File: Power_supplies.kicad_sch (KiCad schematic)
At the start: 54 parts, among them J2 DG35C-B-02P, T1 AOSP21357, T2 MJD32C, U3 MC34063, U31 EL817, U4 MC34063, U5 TLV70233_SOT23-5

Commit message: v2.1 finished
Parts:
- added D101: AOZ8211, _Diodes:AOZ8211, symbol _Diodes:AOZ8211
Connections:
- net 3V3: now also D101.2
- net GND: now also D101.1
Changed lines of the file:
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@@
   (junction (at 182.88 104.14) (diameter 0) (color 0 0 0 0)
   )
+  (junction (at 271.78 62.23) (diameter 0) (color 0 0 0 0)
+  )
   (junction (at 113.03 45.72) (diameter 0) (color 0 0 0 0)
   )
@@
     (stroke (width 0) (type default) (color 0 0 0 0))
   )
+  (wire (pts (xy 271.78 62.23) (xy 276.86 62.23))
+    (stroke (width 0) (type default) (color 0 0 0 0))
+  )
   (wire (pts (xy 138.43 113.03) (xy 135.89 113.03))
     (stroke (width 0) (type default) (color 0 0 0 0))
@@
     (stroke (width 0) (type default) (color 0 0 0 0))
   )
+  (wire (pts (xy 271.78 76.2) (xy 271.78 81.28))
+    (stroke (width 0) (type default) (color 0 0 0 0))
+  )
   (wire (pts (xy 36.83 34.29) (xy 36.83 36.83))
     (stroke (width 0) (type default) (color 0 0 0 0))
@@
     (stroke (width 0) (type default) (color 0 0 0 0))
   )
+  (wire (pts (xy 271.78 62.23) (xy 271.78 68.58))
+    (stroke (width 0) (type default) (color 0 0 0 0))
+  )
   (wire (pts (xy 194.31 62.23) (xy 200.66 62.23))
     (stroke (width 0) (type default) (color 0 0 0 0))
@@
     (stroke (width 0) (type default) (color 0 0 0 0))
   )
-  (wire (pts (xy 256.54 62.23) (xy 266.7 62.23))
+  (wire (pts (xy 256.54 62.23) (xy 271.78 62.23))
     (stroke (width 0) (type default) (color 0 0 0 0))
   )
@@
     (effects (font (size 1.27 1.27)) (justify left))
   )
-  (hierarchical_label "3V3" (shape output) (at 266.7 62.23 0)
+  (hierarchical_label "3V3" (shape output) (at 276.86 62.23 0)
     (effects (font (size 1.27 1.27)) (justify left))
   )
@@
   (symbol (lib_id "Connector:TestPoint") (at 267.97 22.86 0) (unit 1)
     (in_bom yes) (on_board yes)
-    (property "Reference" "TP33" (id 0) (at 269.24 17.78 0)
+    (property "Reference" "TP33" (id 0) (at 267.97 13.97 90)
       (effects (font (size 1.27 1.27)) (justify right))
     )
@@
   (symbol (lib_id "Connector:TestPoint") (at 275.59 22.86 0) (unit 1)
     (in_bom yes) (on_board yes)
-    (property "Reference" "TP41" (id 0) (at 276.86 17.78 0)
+    (property "Reference" "TP41" (id 0) (at 275.59 13.97 90)
       (effects (font (size 1.27 1.27)) (justify right))
     )
@@
   (symbol (lib_id "Connector:TestPoint") (at 264.16 22.86 0) (unit 1)
     (in_bom yes) (on_board yes)
-    (property "Reference" "TP32" (id 0) (at 265.43 17.78 0)
+    (property "Reference" "TP32" (id 0) (at 264.16 13.97 90)
       (effects (font (size 1.27 1.27)) (justify right))
     )
@@
   (symbol (lib_id "Connector:TestPoint") (at 279.4 22.86 0) (unit 1)
     (in_bom yes) (on_board yes)
-    (property "Reference" "TP48" (id 0) (at 280.67 17.78 0)
+    (property "Reference" "TP48" (id 0) (at 279.4 13.97 90)
       (effects (font (size 1.27 1.27)) (justify right))
     )
@@
     )
     (property "Datasheet" "~" (id 3) (at 284.48 22.86 0)
+      (effects (font (size 1.27 1.27)) hide)
+    )
+    (pin "1")
+  )
+  (symbol (lib_id "power:GND") (at 271.78 81.28 0) (unit 1)
+    (in_bom yes) (on_board yes) (fields_autoplaced)
+    (property "Reference" "#PWR0210" (id 0) (at 271.78 87.63 0)
+      (effects (font (size 1.27 1.27)) hide)
+    )
+    (property "Value" "GND" (id 1) (at 271.78 86.36 0))
+    (property "Footprint" "" (id 2) (at 271.78 81.28 0)
+      (effects (font (size 1.27 1.27)) hide)
+    )
+    (property "Datasheet" "" (id 3) (at 271.78 81.28 0)
       (effects (font (size 1.27 1.27)) hide)
     )
@@
   (symbol (lib_id "Connector:TestPoint") (at 271.78 22.86 0) (unit 1)
     (in_bom yes) (on_board yes)
-    (property "Reference" "TP40" (id 0) (at 273.05 17.78 0)
+    (property "Reference" "TP40" (id 0) (at 271.78 13.97 90)
       (effects (font (size 1.27 1.27)) (justify right))
     )
@@
       (effects (font (size 1.27 1.27)) hide)
     )
+    (pin "1")
+    (pin "2")
+  )
+  (symbol (lib_id "_Diodes:AOZ8211") (at 269.24 72.39 90) (unit 1)
+    (in_bom yes) (on_board yes) (fields_autoplaced)
+    (property "Reference" "D101" (id 0) (at 274.32 71.1199 90)
+      (effects (font (size 1.27 1.27)) (justify right))
+    )
+    (property "Value" "AOZ8211" (id 1) (at 274.32 73.6599 90)
+      (effects (font (size 1.27 1.27)) (justify right))
+    )
+    (property "Footprint" "_Diodes:AOZ8211" (id 2) (at 269.24 72.39 0)
+      (effects (font (size 1.27 1.27)) hide)
+    )
+    (property "Datasheet" "" (id 3) (at 269.24 72.39 0)
+      (effects (font (size 1.27 1.27)) hide)
+    )

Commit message: changed power loss detection schematic, changed tvs diodes on other type, added two more caps on 3v3 line, change indicator leds resistors
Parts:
- removed D101: AOZ8211, _Diodes:AOZ8211, symbol _Diodes:AOZ8211
- removed R108, R109: 1k, Resistor_SMD:R_0603_1608Metric_Pad0.98x0.95mm_HandSolder, symbol Device:R
- removed TP9, TP93: TestPoint, TestPoint:TestPoint_THTPad_1.0x1.0mm_Drill0.5mm, symbol Connector:TestPoint
- removed U31: EL817, Package_DIP:DIP-4_W8.89mm_SMDSocket_LongPads, symbol Isolator:EL817
- added C?: 220u, Capacitor_SMD:CP_Elec_6.3x5.4, symbol Device:C_Polarized
- added C? (x2): 330u 6.3V, Capacitor_SMD:CP_Elec_8x6.2, symbol Device:C_Polarized
- added D?: UCLAMP3301D.TCT, _Diodes:UCLAMP3301D.TCT, symbol _Diodes:UCLAMP3301D.TCT
- added D?: B330, Diode_SMD:D_SMA_Handsoldering, symbol Diode:B330
- added R: 100k, Resistor_SMD:R_0603_1608Metric_Pad0.98x0.95mm_HandSolder, symbol Device:R
- added R?: 47k, Resistor_SMD:R_0603_1608Metric_Pad0.98x0.95mm_HandSolder, symbol Device:R
- added R?: 10k, Resistor_SMD:R_0603_1608Metric_Pad0.98x0.95mm_HandSolder, symbol Device:R
- added TP?: TestPoint, TestPoint:TestPoint_THTPad_1.0x1.0mm_Drill0.5mm, symbol Connector:TestPoint
- added U? (x2): AP331A, symbol _IntegratedCircuits:AP331A
- C14: value 100u -> 330u 6.3V
- R12: value 10k -> 36k
- R15: value 3k -> 12k
- R16, R2: value 15k -> 36k
- R6: value 240 -> 240R
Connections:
- net +3V3: now also D?.2 (A), R?.1, U?.5 (V+)
- net 3V3: now also C?.1, C?.1, D?.1
- net GND: now also C?.2, C?.2, C?.2, D?.2, R?.2, U?.2 (V-)
- net POWER_ERROR: now also R?.2, TP?.1, U?.4
- net VDD: now also R.1
- new net 3V_inverting_in: C?.1, D?.1 (K), U?.1 (-)
- new net divider_non_inverting_in: R.2, R?.1, U?.3 (+)
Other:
- note added: "3,3V 300mA"
- note added: "3V"
- note added: "HI - POWER LOSS NOT DETECTED LO - POWER LOSS DETECTED"
- note added: "Open colllector output"
- note added: "~9.5V on power line = power loss detected"
- note removed: "3,3V 200mA"
- note removed: "HI - POWER OFF LO - POWER ON"
- moved on the sheet: C14

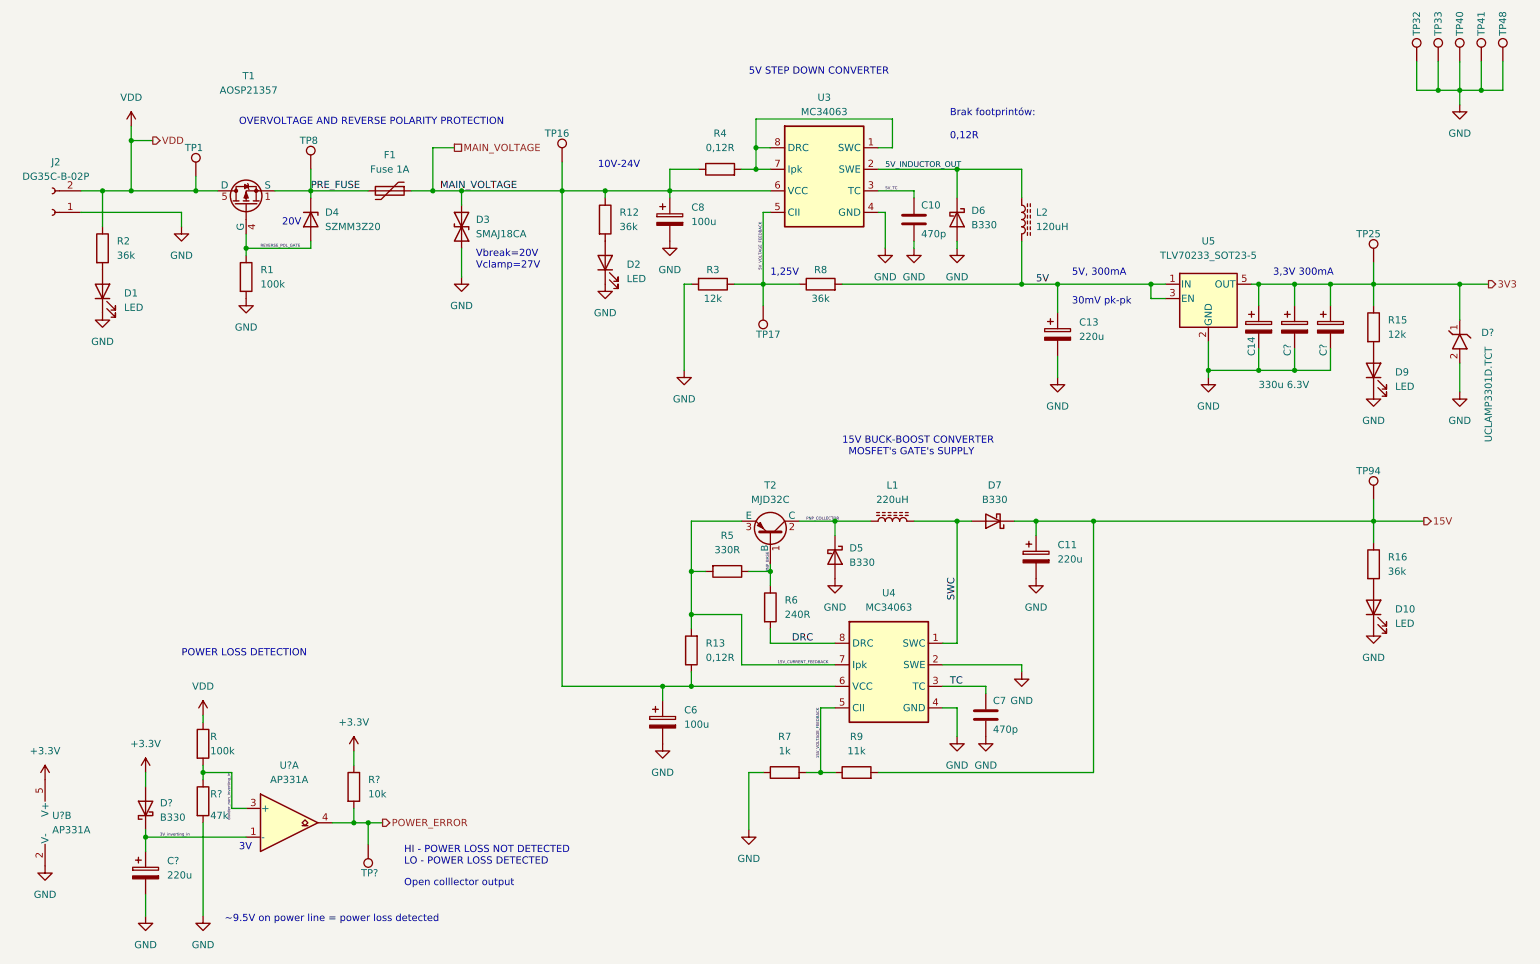
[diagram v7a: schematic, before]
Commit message: updated footprints on board and sgematics
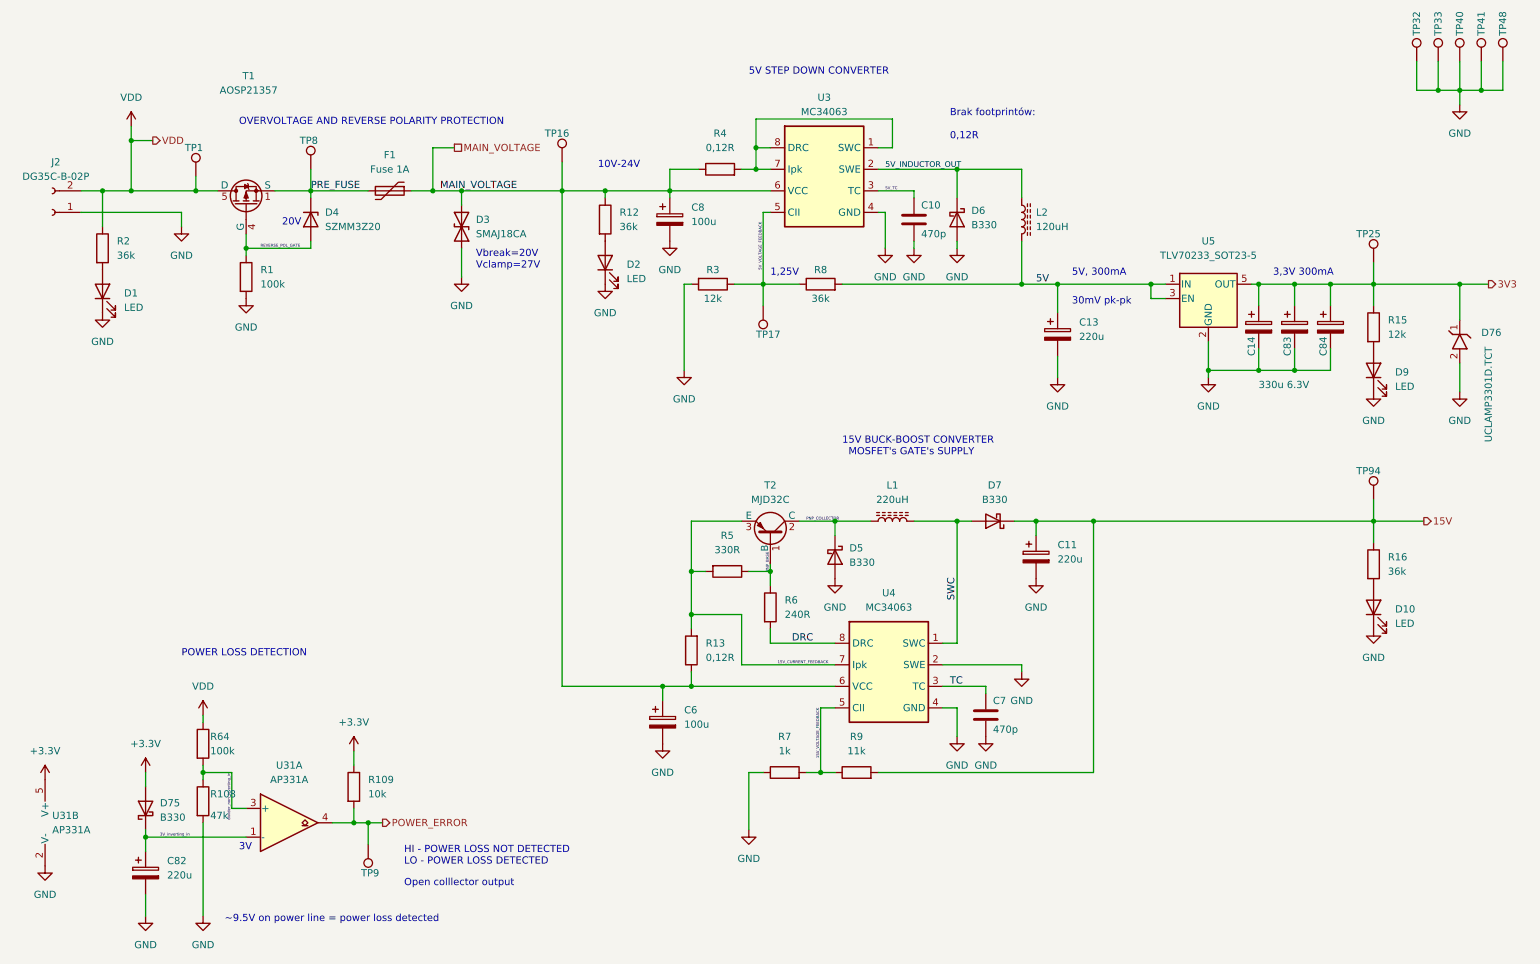
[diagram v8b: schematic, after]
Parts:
- D3: footprint Diode_SMD:D_SMA_Handsoldering -> Diode_THT:D_DO-201AE_P15.24mm_Horizontal
- D5, D6, D7: footprint Diode_SMD:D_SMA_Handsoldering -> Diode_SMD:D_SMC
- D75: renamed from D?; footprint Diode_SMD:D_SMA_Handsoldering -> Diode_SMD:D_SMC
- gave numbers to parts that had none: 8
- renumbered R to R64
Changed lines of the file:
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@@
       (effects (font (size 1.27 1.27)) (justify right))
     )
-    (property "Footprint" "Diode_SMD:D_SMA_Handsoldering" (id 2) (at 100.33 52.07 0)
+    (property "Footprint" "Diode_THT:D_DO-201AE_P15.24mm_Horizontal" (id 2) (at 100.33 52.07 0)
       (effects (font (size 1.27 1.27)) hide)
     )
@@
       (effects (font (size 1.27 1.27)) (justify left))
     )
-    (property "Footprint" "Diode_SMD:D_SMA_Handsoldering" (id 2) (at 156.845 110.49 0)
+    (property "Footprint" "Diode_SMD:D_SMC" (id 2) (at 156.845 110.49 0)
       (effects (font (size 1.27 1.27)) hide)
     )
@@
   (symbol (lib_id "power:VDD") (at 49.53 138.43 0) (unit 1)
     (in_bom yes) (on_board yes) (fields_autoplaced)
-    (property "Reference" "#PWR?" (id 0) (at 49.53 142.24 0)
+    (property "Reference" "#PWR0188" (id 0) (at 49.53 142.24 0)
       (effects (font (size 1.27 1.27)) hide)
     )
@@
   (symbol (lib_id "power:+3.3V") (at 39.37 148.59 0) (unit 1)
     (in_bom yes) (on_board yes) (fields_autoplaced)
-    (property "Reference" "#PWR?" (id 0) (at 39.37 152.4 0)
+    (property "Reference" "#PWR0215" (id 0) (at 39.37 152.4 0)
       (effects (font (size 1.27 1.27)) hide)
     )
@@
   (symbol (lib_id "_IntegratedCircuits:AP331A") (at 21.59 157.48 0) (unit 2)
     (in_bom yes) (on_board yes) (fields_autoplaced)
-    (property "Reference" "U?" (id 0) (at 22.86 156.2099 0)
+    (property "Reference" "U31" (id 0) (at 22.86 156.2099 0)
       (effects (font (size 1.27 1.27)) (justify left))
     )
@@
   (symbol (lib_id "Device:C_Polarized") (at 39.37 166.37 0) (unit 1)
     (in_bom yes) (on_board yes) (fields_autoplaced)
-    (property "Reference" "C?" (id 0) (at 43.18 164.2109 0)
+    (property "Reference" "C82" (id 0) (at 43.18 164.2109 0)
       (effects (font (size 1.27 1.27)) (justify left))
     )
@@
   (symbol (lib_id "power:GND") (at 49.53 173.99 0) (unit 1)
     (in_bom yes) (on_board yes) (fields_autoplaced)
-    (property "Reference" "#PWR?" (id 0) (at 49.53 180.34 0)
+    (property "Reference" "#PWR0191" (id 0) (at 49.53 180.34 0)
       (effects (font (size 1.27 1.27)) hide)
     )
@@
   (symbol (lib_id "power:GND") (at 21.59 165.1 0) (unit 1)
     (in_bom yes) (on_board yes) (fields_autoplaced)
-    (property "Reference" "#PWR?" (id 0) (at 21.59 171.45 0)
+    (property "Reference" "#PWR0217" (id 0) (at 21.59 171.45 0)
       (effects (font (size 1.27 1.27)) hide)
     )
@@
   (symbol (lib_id "power:+3.3V") (at 21.59 149.86 0) (unit 1)
     (in_bom yes) (on_board yes) (fields_autoplaced)
-    (property "Reference" "#PWR?" (id 0) (at 21.59 153.67 0)
+    (property "Reference" "#PWR0216" (id 0) (at 21.59 153.67 0)
       (effects (font (size 1.27 1.27)) hide)
     )
@@
   (symbol (lib_id "Device:C_Polarized") (at 248.92 69.85 0) (unit 1)
     (in_bom yes) (on_board yes)
-    (property "Reference" "C?" (id 0) (at 247.65 74.93 90)
+    (property "Reference" "C84" (id 0) (at 247.65 74.93 90)
       (effects (font (size 1.27 1.27)) (justify left))
     )
@@
   (symbol (lib_id "power:GND") (at 39.37 173.99 0) (unit 1)
     (in_bom yes) (on_board yes) (fields_autoplaced)
-    (property "Reference" "#PWR?" (id 0) (at 39.37 180.34 0)
+    (property "Reference" "#PWR0190" (id 0) (at 39.37 180.34 0)
       (effects (font (size 1.27 1.27)) hide)
     )
@@
   (symbol (lib_id "Device:R") (at 49.53 153.67 0) (unit 1)
     (in_bom yes) (on_board yes)
-    (property "Reference" "R?" (id 0) (at 50.8 152.4 0)
+    (property "Reference" "R108" (id 0) (at 50.8 152.4 0)
       (effects (font (size 1.27 1.27)) (justify left))
     )
@@
   (symbol (lib_id "Device:R") (at 49.53 143.51 0) (unit 1)
     (in_bom yes) (on_board yes)
-    (property "Reference" "R" (id 0) (at 50.8 142.24 0)
+    (property "Reference" "R64" (id 0) (at 50.8 142.24 0)
       (effects (font (size 1.27 1.27)) (justify left))
     )
@@
   (symbol (lib_id "power:+3.3V") (at 76.2 144.78 0) (unit 1)
     (in_bom yes) (on_board yes) (fields_autoplaced)
-    (property "Reference" "#PWR?" (id 0) (at 76.2 148.59 0)
+    (property "Reference" "#PWR0189" (id 0) (at 76.2 148.59 0)
       (effects (font (size 1.27 1.27)) hide)
     )
@@
   (symbol (lib_id "Connector:TestPoint") (at 78.74 161.29 180) (unit 1)
     (in_bom yes) (on_board yes)
-    (property "Reference" "TP?" (id 0) (at 77.47 166.37 0)
+    (property "Reference" "TP9" (id 0) (at 77.47 166.37 0)
       (effects (font (size 1.27 1.27)) (justify right))
     )
@@
   (symbol (lib_id "_IntegratedCircuits:AP331A") (at 64.77 157.48 0) (unit 1)
     (in_bom yes) (on_board yes) (fields_autoplaced)
-    (property "Reference" "U?" (id 0) (at 64.77 147.32 0))
+    (property "Reference" "U31" (id 0) (at 64.77 147.32 0))
     (property "Value" "AP331A" (id 1) (at 64.77 149.86 0))
     (property "Footprint" "" (id 2) (at 64.77 157.48 0)
@@
   (symbol (lib_id "_Diodes:UCLAMP3301D.TCT") (at 271.78 80.01 0) (unit 1)
     (in_bom yes) (on_board yes)
-    (property "Reference" "D?" (id 0) (at 275.59 70.7955 0)
+    (property "Reference" "D76" (id 0) (at 275.59 70.7955 0)
       (effects (font (size 1.27 1.27)) (justify left))
     )
@@
   (symbol (lib_id "Diode:B330") (at 39.37 154.94 90) (unit 1)
     (in_bom yes) (on_board yes) (fields_autoplaced)
-    (property "Reference" "D?" (id 0) (at 41.91 153.9874 90)
+    (property "Reference" "D75" (id 0) (at 41.91 153.9874 90)
       (effects (font (size 1.27 1.27)) (justify right))
     )
@@
       (effects (font (size 1.27 1.27)) (justify right))
     )
-    (property "Footprint" "Diode_SMD:D_SMA_Handsoldering" (id 2) (at 43.815 154.94 0)
+    (property "Footprint" "Diode_SMD:D_SMC" (id 2) (at 43.815 154.94 0)
       (effects (font (size 1.27 1.27)) hide)
     )
@@
     (property "Reference" "D7" (id 0) (at 189.5475 97.79 0))
     (property "Value" "B330" (id 1) (at 189.5475 100.33 0))
-    (property "Footprint" "Diode_SMD:D_SMA_Handsoldering" (id 2) (at 189.23 99.695 0)
+    (property "Footprint" "Diode_SMD:D_SMC" (id 2) (at 189.23 99.695 0)
       (effects (font (size 1.27 1.27)) hide)
     )
@@
       (effects (font (size 1.27 1.27)) (justify left))
     )
-    (property "Footprint" "Diode_SMD:D_SMA_Handsoldering" (id 2) (at 178.435 50.8 0)
+    (property "Footprint" "Diode_SMD:D_SMC" (id 2) (at 178.435 50.8 0)
       (effects (font (size 1.27 1.27)) hide)
     )
@@
   (symbol (lib_id "Device:C_Polarized") (at 242.57 69.85 0) (unit 1)
     (in_bom yes) (on_board yes)
-    (property "Reference" "C?" (id 0) (at 241.3 74.93 90)
+    (property "Reference" "C83" (id 0) (at 241.3 74.93 90)
       (effects (font (size 1.27 1.27)) (justify left))
     )
@@
   (symbol (lib_id "Device:R") (at 76.2 151.13 0) (unit 1)
     (in_bom yes) (on_board yes) (fields_autoplaced)
-    (property "Reference" "R?" (id 0) (at 78.74 149.8599 0)
-      (effects (font (size 1.27 1.27)) (justify left))
-    )
+    (property "Reference" "R109" (id 0) (at 78.74 149.8599 0)
+      (effects (font (size 1.27 1.27)) (justify left))
+    )
